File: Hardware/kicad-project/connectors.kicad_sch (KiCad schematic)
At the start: 22 parts, among them CN10 Conn_02x17_Odd_Even, CN7 Conn_02x10_Odd_Even, CN8 Conn_02x08_Odd_Even, CN9 Conn_02x15_Odd_Even, J1 Brake connector, J2 Conn_01x08, J3 PWM module connector, J5 UART Connector, Q1 Q_NMOS_DGS

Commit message: hw: schematic update
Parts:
- removed R2: 1M, Resistor_SMD:R_0603_1608Metric, symbol Device:R
- removed TP?: TestPoint, TestPoint:TestPoint_Pad_D2.0mm, symbol Connector:TestPoint
- added D7, D8: LED, LED_SMD:LED_0603_1608Metric, symbol Device:LED
- added D?: DIODE, Diode_SMD:D_SOD-323, symbol Simulation_SPICE:DIODE
- added R18: 510, Resistor_SMD:R_0603_1608Metric, symbol Device:R
- added R19: 330, Resistor_SMD:R_0603_1608Metric, symbol Device:R
- Q1: footprint (none) -> Package_TO_SOT_SMD:TO-252-2
- R1: value 1M -> 10k
- gave numbers to parts that had none: 6
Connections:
- net BRAKE_PWM is gone; now on net PWM_BRAKE: R3.1
- net +24V: now also D?.1 (A); no longer D1.2 (K), J1.1 (Pin_1)
- net +5V: no longer R1.1
- net GND: now also R1.1, R18.2, R19.2
- net at Q1.2 (G), R3.2: now also R1.2
- net LED1: now reaches CN9.16 (Pin_16)
- net LED1: now also D7.2 (A)
- net LED2: now reaches CN9.18 (Pin_18)
- net LED2: now also D8.2 (A)
- removed net VREF_2V5: J2.7 (Pin_7), J2.8 (Pin_8), R1.2
- new net: D1.2 (K), D?.2 (K), J1.1 (Pin_1)
- new net: D8.1 (K), R19.1
- new net: D7.1 (K), R18.1
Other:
- note added: "LED"
- title: (none) -> STB
- moved on the sheet: R3, TP1, TP2, TP3, TP4, TP5

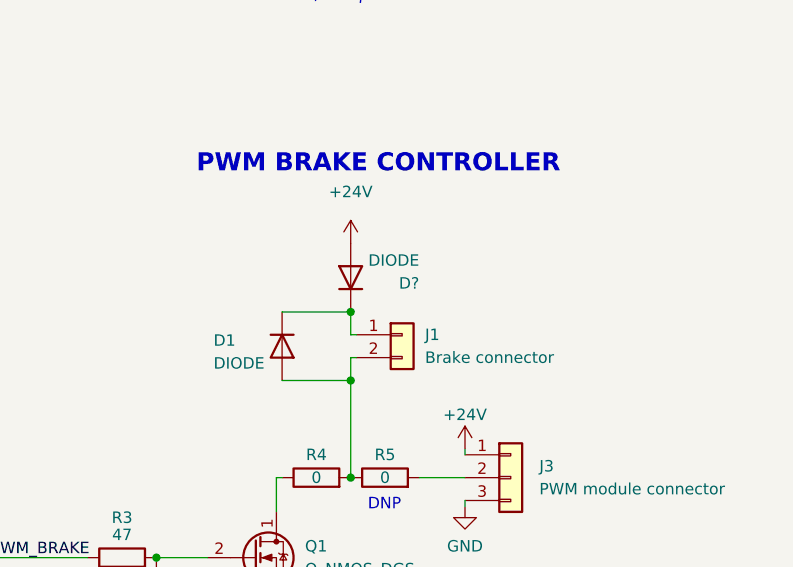
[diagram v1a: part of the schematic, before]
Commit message: hw: dix schematic conflict
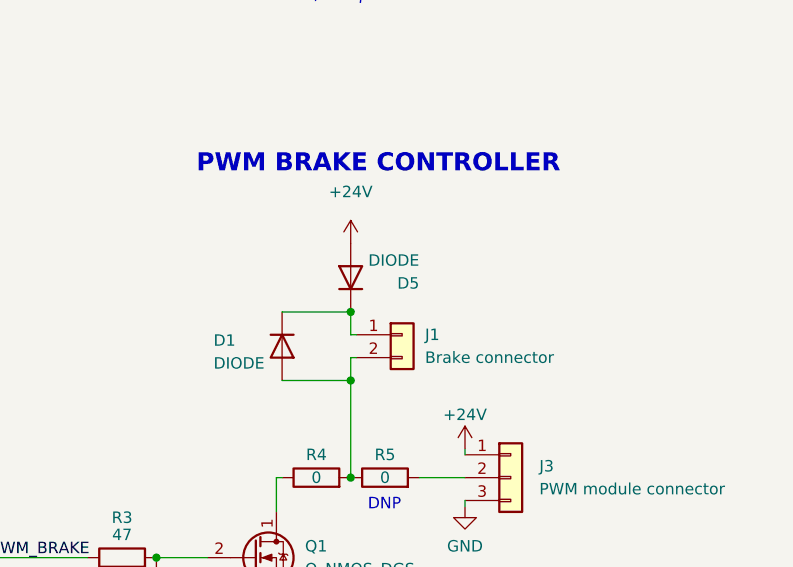
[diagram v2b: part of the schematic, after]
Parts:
- gave numbers to parts that had none: 1
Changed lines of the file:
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@@
   (symbol (lib_id "Simulation_SPICE:DIODE") (at 222.25 109.22 270) (unit 1)
     (in_bom yes) (on_board yes)
-    (property "Reference" "D?" (id 0) (at 229.87 109.855 90)
+    (property "Reference" "D5" (id 0) (at 229.87 109.855 90)
       (effects (font (size 1.27 1.27)) (justify right))
     )
